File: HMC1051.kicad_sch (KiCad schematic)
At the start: 40 parts, among them U1 LMV324

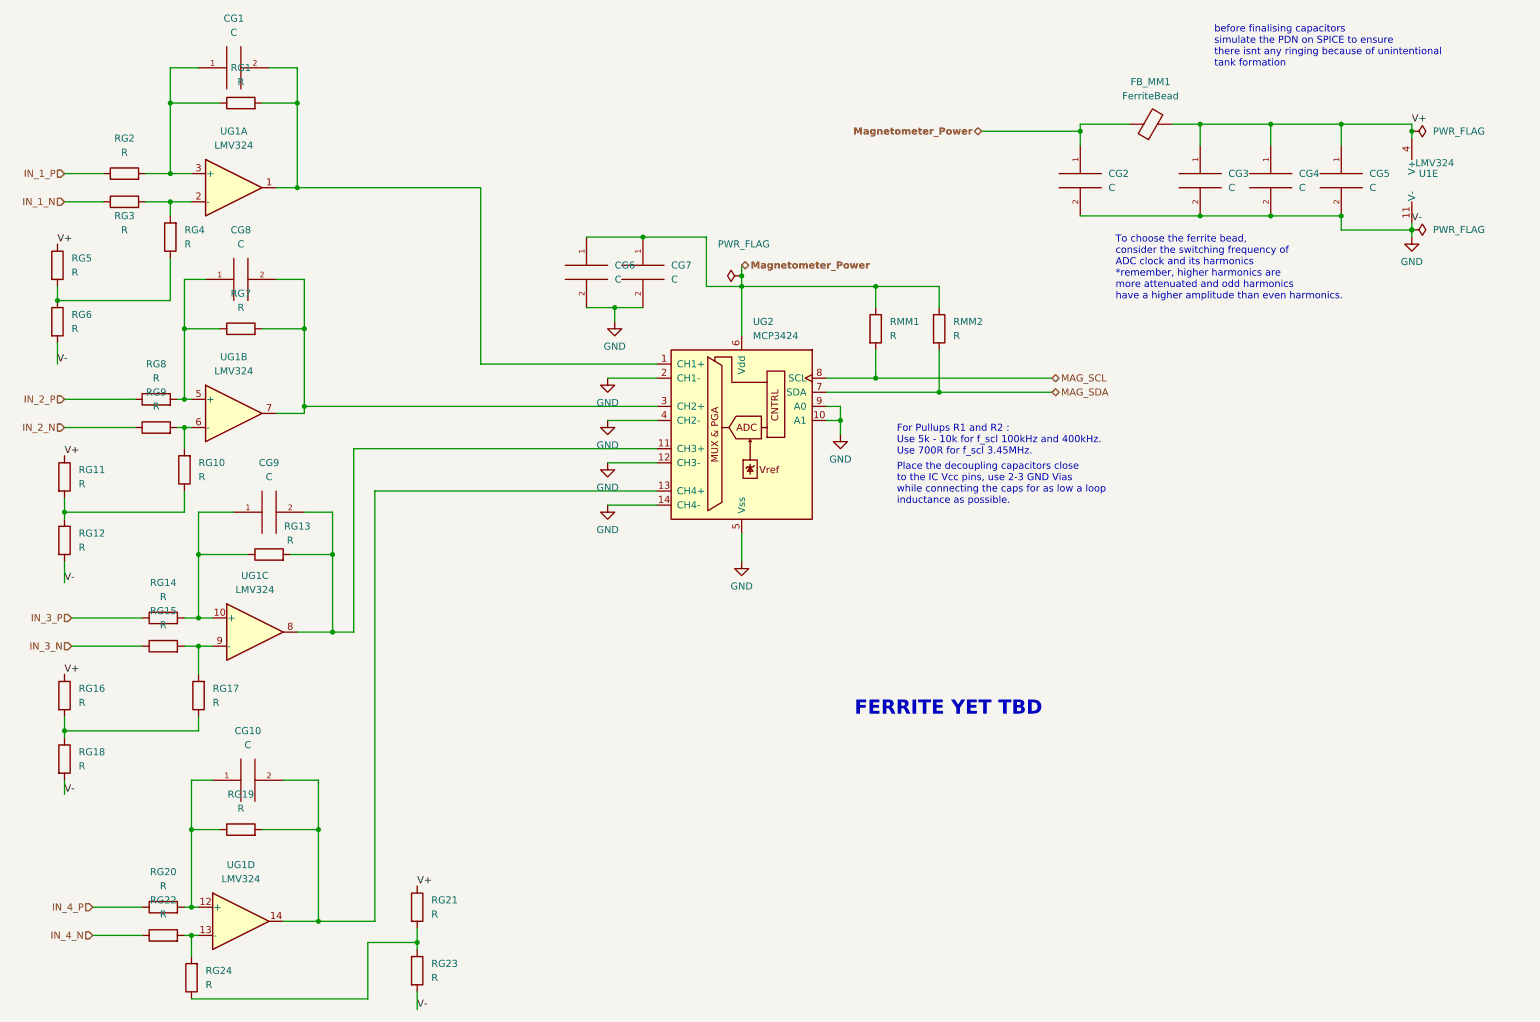
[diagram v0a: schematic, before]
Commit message: Page settings changed. Added some testpoints. Some comments are made.
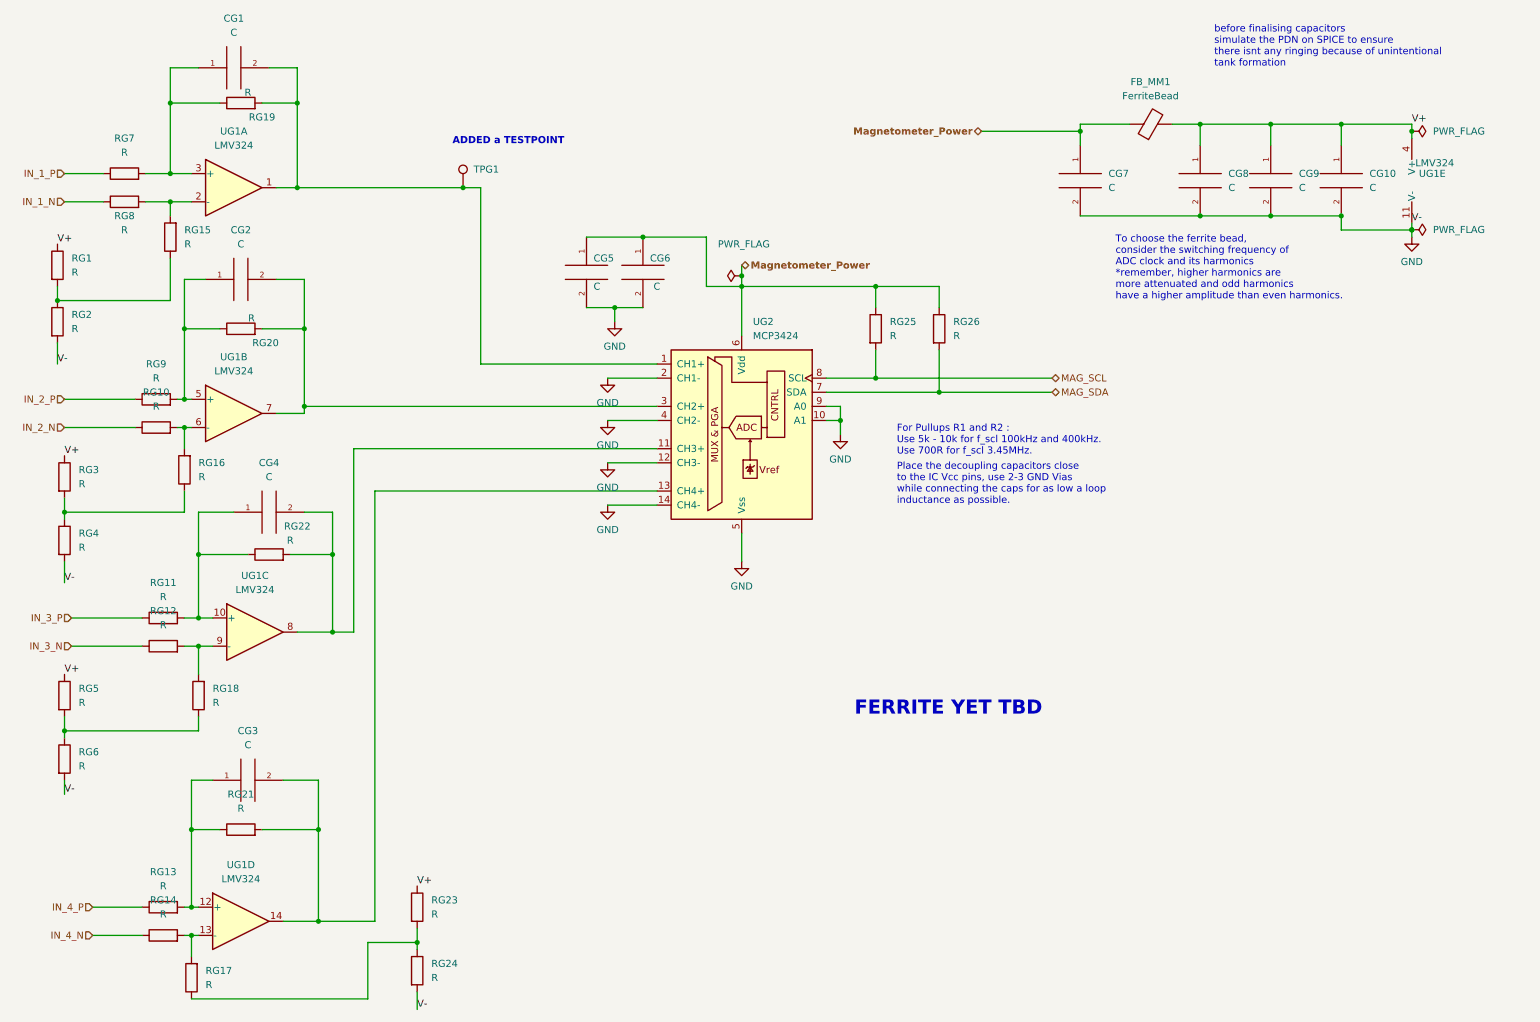
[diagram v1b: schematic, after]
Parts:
- added TPG1: TestPoint, TestPoint:TestPoint_Plated_Hole_D2.0mm, symbol Connector:TestPoint
- renumbered CG5 to CG10, CG8 to CG2, CG10 to CG3, CG9 to CG4, CG6 to CG5, CG7 to CG6, CG2 to CG7, CG3 to CG8, CG4 to CG9, RG5 to RG1, RG9 to RG10, RG14 to RG11, RG15 to RG12, RG20 to RG13, RG22 to RG14, RG4 to RG15, RG10 to RG16, RG24 to RG17, RG17 to RG18, RG1 to RG19, RG6 to RG2, RG7 to RG20, RG19 to RG21, RG13 to RG22, RG21 to RG23, RG23 to RG24, RMM1 to RG25, RMM2 to RG26, RG11 to RG3, RG12 to RG4, RG16 to RG5, RG18 to RG6, RG2 to RG7, RG3 to RG8, RG8 to RG9, U1 to UG1
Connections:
- net at CG1.2, RG19.2, UG1.1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: now also TPG1.1
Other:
- note added: "ADDED a TESTPOINT"

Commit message: I2C lines are pulled up
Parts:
- removed RG25, RG26: R, symbol Device:R
- added TPG1, TPG2: TestPoint, TestPoint:TestPoint_Plated_Hole_D2.0mm, symbol Connector:TestPoint
- CG1, CG10, CG2, CG3, CG4, CG7, CG8, CG9: footprint (none) -> Capacitor_SMD:C_0603_1608Metric
- CG5: value C -> 0.1u; footprint (none) -> Capacitor_SMD:C_0603_1608Metric
- CG6: value C -> 10u; footprint (none) -> Capacitor_Tantalum_SMD:CP_EIA-6032-28_Kemet-C_Pad2.25x2.35mm_HandSolder
- RG1, RG10, RG11, RG12, RG13, RG14, RG15, RG16, RG17, RG18, RG19, RG2, RG20, RG21, RG22, RG23, RG24, RG3, RG4, RG5, RG6, RG7, RG8, RG9: footprint (none) -> Resistor_SMD:R_0603_1608Metric
- renumbered FB_MM1 to FBG1, TPG1 to TPG3
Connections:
- net IN_4_N: now also TPG2.1
- net IN_4_P: now also TPG1.1

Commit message: Finalisations done, please produce BOM and fabricate
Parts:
- removed FBG1: FerriteBead, symbol Device:FerriteBead
- added RGFB: 0, symbol Device:R
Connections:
- net Magnetometer_Power: now also RGFB.1
- net V+: now also RGFB.2
- net at CG3.2, RG21.2, UG1.14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: now also TPG3.1
- net at CG1.2, RG19.2, UG1.1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: no longer TPG3.1
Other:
- note added: "DNP"
- moved on the sheet: TPG3
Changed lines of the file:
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@@
   (junction (at 147.32 66.04) (diameter 0) (color 0 0 0 0)
   )
+  (junction (at 96.52 102.87) (diameter 0) (color 0 0 0 0)
+  )
   (junction (at 267.97 38.1) (diameter 0) (color 0 0 0 0)
   )
@@
   (junction (at 44.45 50.8) (diameter 0) (color 0 0 0 0)
   )
-  (junction (at 97.155 48.26) (diameter 0) (color 0 0 0 0)
-  )
   (junction (at 33.655 177.8) (diameter 0) (color 0 0 0 0)
   )
@@
     (stroke (width 0) (type default) (color 0 0 0 0))
   )
+  (wire (pts (xy 96.52 102.87) (xy 96.52 111.76))
+    (stroke (width 0) (type default) (color 0 0 0 0))
+  )
   (wire (pts (xy 81.28 180.34) (xy 71.12 180.34))
     (stroke (width 0) (type default) (color 0 0 0 0))
@@
     (stroke (width 0) (type default) (color 0 0 0 0))
   )
+  (wire (pts (xy 96.52 102.87) (xy 132.08 102.87))
+    (stroke (width 0) (type default) (color 0 0 0 0))
+  )
   (wire (pts (xy 33.655 177.8) (xy 39.37 177.8))
     (stroke (width 0) (type default) (color 0 0 0 0))
   )
-  (wire (pts (xy 81.28 102.87) (xy 132.08 102.87))
+  (wire (pts (xy 81.28 102.87) (xy 96.52 102.87))
     (stroke (width 0) (type default) (color 0 0 0 0))
   )
@@
     (stroke (width 0) (type default) (color 0 0 0 0))
   )
-  (wire (pts (xy 100.33 48.26) (xy 97.155 48.26))
+  (wire (pts (xy 67.31 48.26) (xy 100.33 48.26))
     (stroke (width 0) (type default) (color 0 0 0 0))
   )
@@
     (stroke (width 0) (type default) (color 0 0 0 0))
   )
-  (wire (pts (xy 97.155 48.26) (xy 67.31 48.26))
-    (stroke (width 0) (type default) (color 0 0 0 0))
-  )
   (wire (pts (xy 44.45 26.67) (xy 44.45 33.02))
     (stroke (width 0) (type default) (color 0 0 0 0))
@@
     (stroke (width 0) (type default) (color 0 0 0 0))
   )
+  (wire (pts (xy 106.68 111.76) (xy 96.52 111.76))
+    (stroke (width 0) (type default) (color 0 0 0 0))
+  )
   (wire (pts (xy 48.26 177.8) (xy 49.53 177.8))
     (stroke (width 0) (type default) (color 0 0 0 0))
@@
   (wire (pts (xy 48.26 194.31) (xy 80.01 194.31))
     (stroke (width 0) (type default) (color 0 0 0 0))
+  )
+  (text "DNP" (at 46.99 96.52 180)
+    (effects (font (size 1.27 1.27) bold italic) (justify right bottom))
+  )
+  (text "DNP" (at 38.1 50.8 180)
+    (effects (font (size 1.27 1.27) bold italic) (justify right bottom))
+  )
+  (text "DNP" (at 41.91 59.69 180)
+    (effects (font (size 1.27 1.27) bold italic) (justify right bottom))
+  )
+  (text "DNP" (at 97.79 191.77 180)
+    (effects (font (size 1.27 1.27) bold italic) (justify right bottom))
   )
   (text "For Pullups R1 and R2 :\nUse 5k - 10k for f_scl 100kHz and 400kHz.\nUse 700R for f_scl 3.45MHz."
@@
     (effects (font (size 1.27 1.27)) (justify left bottom))
   )
+  (text "DNP" (at 66.04 152.4 180)
+    (effects (font (size 1.27 1.27) bold italic) (justify right bottom))
+  )
+  (text "DNP" (at 39.37 123.19 180)
+    (effects (font (size 1.27 1.27) bold italic) (justify right bottom))
+  )
+  (text "DNP" (at 39.37 180.34 180)
+    (effects (font (size 1.27 1.27) bold italic) (justify right bottom))
+  )
+  (text "DNP" (at 46.99 140.97 180)
+    (effects (font (size 1.27 1.27) bold italic) (justify right bottom))
+  )
+  (text "DNP" (at 66.04 118.11 180)
+    (effects (font (size 1.27 1.27) bold italic) (justify right bottom))
+  )
+  (text "DNP" (at 62.23 167.64 180)
+    (effects (font (size 1.27 1.27) bold italic) (justify right bottom))
+  )
+  (text "DNP" (at 60.96 77.47 180)
+    (effects (font (size 1.27 1.27) bold italic) (justify right bottom))
+  )
   (text "FERRITE YET TBD" (at 167.64 143.51 0)
     (effects (font (size 2.54 2.54) (thickness 0.508) bold) (justify left bottom))
@@
   (text "ADDED a TESTPOINT\n" (at 95.25 40.64 0)
     (effects (font (size 1.27 1.27) bold) (justify left bottom))
+  )
+  (text "DNP" (at 30.48 101.6 180)
+    (effects (font (size 1.27 1.27) bold italic) (justify right bottom))
+  )
+  (text "DNP" (at 44.45 134.62 180)
+    (effects (font (size 1.27 1.27) bold italic) (justify right bottom))
+  )
+  (text "DNP" (at 63.5992 68.3983 180)
+    (effects (font (size 1.27 1.27) bold italic) (justify right bottom))
+  )
+  (text "DNP" (at 67.31 104.14 180)
+    (effects (font (size 1.27 1.27) bold italic) (justify right bottom))
+  )
+  (text "DNP" (at 22.86 72.39 180)
+    (effects (font (size 1.27 1.27) bold italic) (justify right bottom))
+  )
+  (text "DNP" (at 22.86 140.97 180)
+    (effects (font (size 1.27 1.27) bold italic) (justify right bottom))
+  )
+  (text "DNP" (at 35.7804 43.9447 180)
+    (effects (font (size 1.27 1.27) bold italic) (justify right bottom))
+  )
+  (text "DNP" (at 40.64 190.5 180)
+    (effects (font (size 1.27 1.27) bold italic) (justify right bottom))
   )
   (text "before finalising capacitors \nsimulate the PDN on SPICE to ensure \nthere isnt any ringing because of unintentional \ntank formation\n"
@@
     (effects (font (size 1.27 1.27)) (justify left bottom))
   )
+  (text "DNP" (at 58.42 22.86 180)
+    (effects (font (size 1.27 1.27) bold italic) (justify right bottom))
+  )
+  (text "DNP" (at 97.79 180.34 180)
+    (effects (font (size 1.27 1.27) bold italic) (justify right bottom))
+  )
+  (text "DNP" (at 22.86 63.5 180)
+    (effects (font (size 1.27 1.27) bold italic) (justify right bottom))
+  )
+  (text "DNP" (at 39.37 83.82 180)
+    (effects (font (size 1.27 1.27) bold italic) (justify right bottom))
+  )
+  (text "DNP" (at 40.64 93.98 180)
+    (effects (font (size 1.27 1.27) bold italic) (justify right bottom))
+  )
   (text "To choose the ferrite bead, \nconsider the switching frequency of \nADC clock and its harmonics \n*remember, higher harmonics are \nmore attenuated and odd harmonics \nhave a higher amplitude than even harmonics. "
     (at 214.63 68.58 0)
     (effects (font (size 1.27 1.27)) (justify left bottom))
+  )
+  (text "DNP" (at 22.86 151.13 180)
+    (effects (font (size 1.27 1.27) bold italic) (justify right bottom))
+  )
+  (text "DNP" (at 61.6923 31.157 180)
+    (effects (font (size 1.27 1.27) bold italic) (justify right bottom))
+  )
+  (text "DNP" (at 33.02 111.76 180)
+    (effects (font (size 1.27 1.27) bold italic) (justify right bottom))
   )
   (label "V+" (at 25.4 96.52 0)
@@
     (pin "2")
   )
-  (symbol (lib_id "Connector:TestPoint") (at 97.155 48.26 0) (unit 1)
-    (in_bom yes) (on_board yes) (fields_autoplaced)
-    (property "Reference" "TPG3" (id 0) (at 99.06 44.9579 0)
-      (effects (font (size 1.27 1.27)) (justify left))
-    )
-    (property "Value" "TestPoint" (id 1) (at 99.06 46.2279 0)
+  (symbol (lib_id "Connector:TestPoint") (at 106.68 111.76 0) (unit 1)
+    (in_bom yes) (on_board yes) (fields_autoplaced)
+    (property "Reference" "TPG3" (id 0) (at 108.585 108.4579 0)
+      (effects (font (size 1.27 1.27)) (justify left))
+    )
+    (property "Value" "TestPoint" (id 1) (at 108.585 109.7279 0)
       (effects (font (size 1.27 1.27)) (justify left) hide)
     )
-    (property "Footprint" "TestPoint:TestPoint_Plated_Hole_D2.0mm" (id 2) (at 102.235 48.26 0)
-      (effects (font (size 1.27 1.27)) hide)
-    )
-    (property "Datasheet" "~" (id 3) (at 102.235 48.26 0)
+    (property "Footprint" "TestPoint:TestPoint_Plated_Hole_D2.0mm" (id 2) (at 111.76 111.76 0)
+      (effects (font (size 1.27 1.27)) hide)
+    )
+    (property "Datasheet" "~" (id 3) (at 111.76 111.76 0)
       (effects (font (size 1.27 1.27)) hide)
     )
@@
     )
     (property "Datasheet" "~" (id 3) (at 62.23 106.68 0)
+      (effects (font (size 1.27 1.27)) hide)
+    )
+    (pin "1")
+    (pin "2")
+  )
+  (symbol (lib_id "Device:R") (at 220.98 36.83 90) (unit 1)
+    (in_bom yes) (on_board yes) (fields_autoplaced)
+    (property "Reference" "RGFB" (id 0) (at 220.98 30.48 90))
+    (property "Value" "0" (id 1) (at 220.98 33.02 90))
+    (property "Footprint" "" (id 2) (at 220.98 38.608 90)
+      (effects (font (size 1.27 1.27)) hide)
+    )
+    (property "Datasheet" "~" (id 3) (at 220.98 36.83 0)
       (effects (font (size 1.27 1.27)) hide)
     )
@@
     (pin "4")
   )
-  (symbol (lib_id "Device:FerriteBead") (at 220.98 36.83 90) (unit 1)
-    (in_bom yes) (on_board yes) (fields_autoplaced)
-    (property "Reference" "FBG1" (id 0) (at 220.9292 29.21 90))
-    (property "Value" "FerriteBead" (id 1) (at 220.9292 31.75 90))
-    (property "Footprint" "" (id 2) (at 220.98 38.608 90)
-      (effects (font (size 1.27 1.27)) hide)
-    )
-    (property "Datasheet" "~" (id 3) (at 220.98 36.83 0)
-      (effects (font (size 1.27 1.27)) hide)
-    )
-    (pin "1")
-    (pin "2")
-  )
   (symbol (lib_id "Device:R") (at 49.53 139.7 180) (unit 1)

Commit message: Final Schematic
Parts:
- RG1, RG10, RG11, RG12, RG13, RG14, RG15, RG16, RG17, RG18, RG19, RG2, RG20, RG21, RG22, RG23, RG24, RG3, RG4, RG5, RG6, RG7, RG8, RG9: footprint Resistor_SMD:R_0603_1608Metric -> Resistor_SMD:R_0603_1608Metric_Pad0.98x0.95mm_HandSolder
- RGFB1: renamed from RGFB; footprint (none) -> Resistor_SMD:R_0805_2012Metric_Pad1.20x1.40mm_HandSolder
- UG1: footprint (none) -> LMV324AQDRQ1:SOIC127P600X175-14N
- UG2: footprint (none) -> MCP3424-E_SL:SOIC127P600X175-14N
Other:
- note added: "Decouple with 0.1uF Ceramic cap and 10uF Tantalum cap"
- note removed: "ADDED a TESTPOINT"
- note removed: "FERRITE YET TBD"
